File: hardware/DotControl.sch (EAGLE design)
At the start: 44 parts, among them CN1 1X4-BIG, IC1 MCP1703CB, J3 USB-MICROB, SW2 Previous, SW5 Previous, SW6 Next, SW8 Ok, U1 ATMEGA328P-MU-QFN32, U2 TMP102, U3 ATSHA204-TSU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

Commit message: Clean warnings
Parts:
- added C2: 1uF, rcl:C-EUC0603
- BAT1: value (none) -> 3V ML2032
- C1: value (none) -> 1uF
- D1, D2: value (none) -> MM5Z3V3
- R3, R4: value (none) -> 47Ω
- R5: value (none) -> 1.5kΩ
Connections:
- net +5V: now also C2.1
- net GND: now also C2.2
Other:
- moved on the sheet: SJ2
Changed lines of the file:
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@@
 <part name="+3V19" library="supply1" deviceset="+3V3" device=""/>
 <part name="P+4" library="supply1" deviceset="+5V" device=""/>
-<part name="C1" library="rcl" deviceset="C-EU" device="C0603"/>
+<part name="C1" library="rcl" deviceset="C-EU" device="C0603" value="1uF"/>
 <part name="JP3" library="adafruit" deviceset="PINHD-1X6" device=""/>
 <part name="+3V6" library="supply1" deviceset="+3V3" device=""/>
@@
 <part name="JP1" library="adafruit" deviceset="PINHD-1X8" device="CLEANBIG"/>
 <part name="SUPPLY8" library="supply2" deviceset="GND" device=""/>
-<part name="BAT1" library="Battery" deviceset="BATTERY" device="20PTH"/>
+<part name="BAT1" library="Battery" deviceset="BATTERY" device="20PTH" value="3V ML2032"/>
 <part name="+3V14" library="supply1" deviceset="+3V3" device=""/>
 <part name="LED1" library="led" deviceset="GM1WA55311A" device=""/>
@@
 <part name="SJ2" library="SparkFun" deviceset="SOLDERJUMPER" device="TRACE"/>
 <part name="+3V9" library="supply1" deviceset="+3V3" device=""/>
-<part name="D1" library="diode" deviceset="DIODE-" device="SOD523"/>
-<part name="D2" library="diode" deviceset="DIODE-" device="SOD523"/>
+<part name="D1" library="diode" deviceset="DIODE-" device="SOD523" value="MM5Z3V3"/>
+<part name="D2" library="diode" deviceset="DIODE-" device="SOD523" value="MM5Z3V3"/>
 <part name="SUPPLY14" library="supply2" deviceset="GND" device=""/>
-<part name="R3" library="rcl" deviceset="R-EU_" device="R0603"/>
-<part name="R4" library="rcl" deviceset="R-EU_" device="R0603"/>
-<part name="R5" library="rcl" deviceset="R-EU_" device="R0603"/>
+<part name="R3" library="rcl" deviceset="R-EU_" device="R0603" value="47Ω"/>
+<part name="R4" library="rcl" deviceset="R-EU_" device="R0603" value="47Ω"/>
+<part name="R5" library="rcl" deviceset="R-EU_" device="R0603" value="1.5kΩ"/>
 <part name="P+1" library="supply1" deviceset="+5V" device=""/>
 <part name="X1" library="adafruit" deviceset="ANTENNA_U.FL" device=""/>
@@
 <part name="Q1" library="adafruit" deviceset="MOSFET-N" device="REFLOW"/>
 <part name="IC1" library="linear" deviceset="MCP1703" device="CB"/>
+<part name="C2" library="rcl" deviceset="C-EU" device="C0603" value="1uF"/>
 </parts>
 <sheets>
@@
 <instance part="+3V10" gate="G$1" x="228.6" y="63.5"/>
 <instance part="SUPPLY5" gate="GND" x="228.6" y="53.34"/>
-<instance part="SJ2" gate="1" x="217.17" y="34.29" rot="R180"/>
+<instance part="SJ2" gate="1" x="422.91" y="240.03" rot="R180"/>
 <instance part="+3V9" gate="G$1" x="172.72" y="149.86"/>
 <instance part="D1" gate="G$1" x="322.58" y="99.06" rot="R90"/>
@@
 <instance part="Q1" gate="G$1" x="144.78" y="149.86" rot="R270"/>
 <instance part="IC1" gate="G$1" x="172.72" y="205.74"/>
+<instance part="C2" gate="G$1" x="160.02" y="203.2"/>
 </instances>
 <busses>
@@
 <wire x1="172.72" y1="198.12" x2="172.72" y2="195.58" width="0.1524" layer="91"/>
 <junction x="172.72" y="195.58"/>
+<pinref part="C2" gate="G$1" pin="2"/>
+<wire x1="160.02" y1="198.12" x2="160.02" y2="195.58" width="0.1524" layer="91"/>
+<wire x1="160.02" y1="195.58" x2="172.72" y2="195.58" width="0.1524" layer="91"/>
 </segment>
 <segment>
@@
 <pinref part="P+4" gate="1" pin="+5V"/>
 <wire x1="152.4" y1="210.82" x2="152.4" y2="205.74" width="0.1524" layer="91"/>
-<wire x1="152.4" y1="205.74" x2="162.56" y2="205.74" width="0.1524" layer="91"/>
+<wire x1="152.4" y1="205.74" x2="160.02" y2="205.74" width="0.1524" layer="91"/>
 <pinref part="IC1" gate="G$1" pin="VI"/>
+<pinref part="C2" gate="G$1" pin="1"/>
+<wire x1="160.02" y1="205.74" x2="162.56" y2="205.74" width="0.1524" layer="91"/>
+<junction x="160.02" y="205.74"/>
 </segment>
 <segment>
@@
 </sheet>
 </sheets>
+<errors>
+</errors>
 </schematic>
 </drawing>

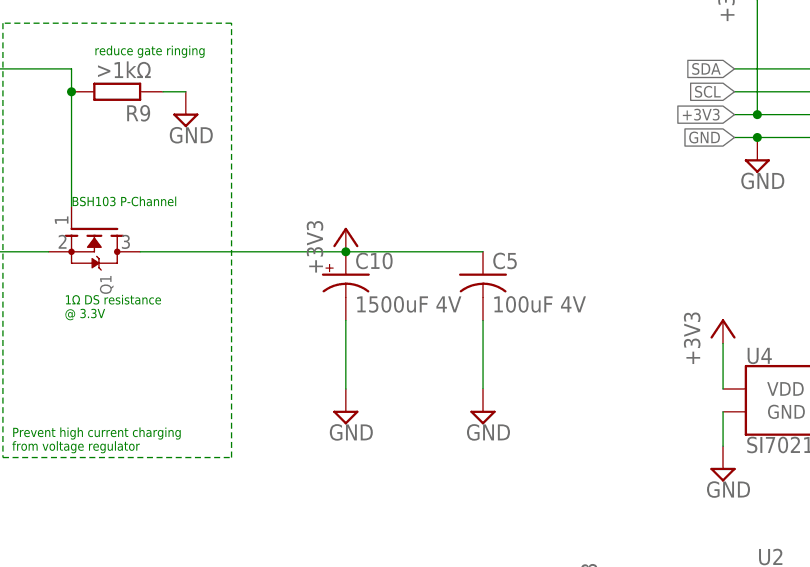
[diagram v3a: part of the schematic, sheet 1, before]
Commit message: 2x100uF instead of 1x1000uF
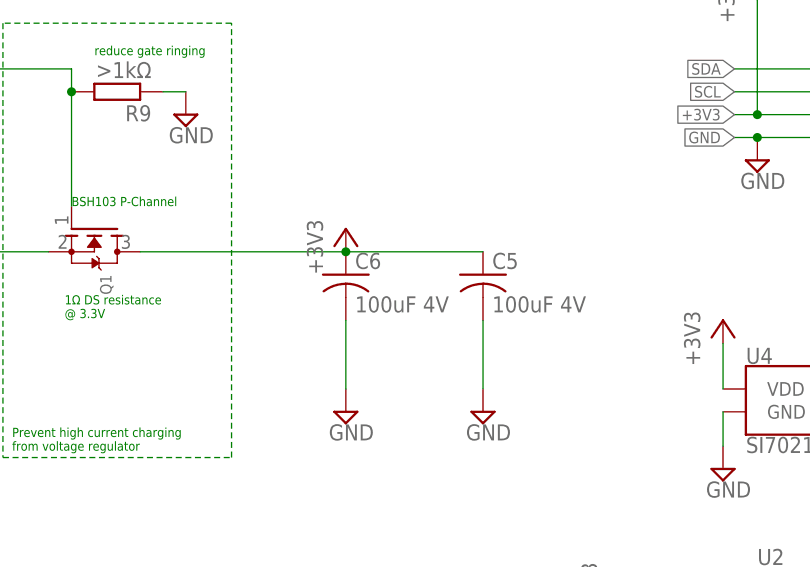
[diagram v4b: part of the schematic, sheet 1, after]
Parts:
- removed C10: 1500uF 4V, adafruit:CPOL-USCT7343
- added C6: 100uF 4V, adafruit:C-USC3216
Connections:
- net +3V3: now also C6.1; no longer C10.+
- net GND: now also C6.2; no longer C10.-
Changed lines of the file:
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@@
 <part name="+3V12" library="supply1" deviceset="+3V3" device=""/>
 <part name="SUPPLY11" library="supply2" deviceset="GND" device=""/>
-<part name="C10" library="adafruit" deviceset="CPOL-US" device="CT7343" value="1500uF 4V"/>
 <part name="SUPPLY16" library="supply2" deviceset="GND" device=""/>
 <part name="U5" library="SparkFun-Sensors" deviceset="MPU-9250" device="" value="9DoF IMU"/>
@@
 <part name="IC1" library="linear" deviceset="MCP1703" device="CB"/>
 <part name="C2" library="rcl" deviceset="C-EU" device="C0603" value="1uF"/>
+<part name="C6" library="adafruit" deviceset="C-US" device="C3216" value="100uF 4V"/>
 </parts>
 <sheets>
@@
 <instance part="+3V12" gate="G$1" x="214.63" y="139.7"/>
 <instance part="SUPPLY11" gate="GND" x="214.63" y="123.19"/>
-<instance part="C10" gate="G$1" x="172.72" y="144.78"/>
 <instance part="SUPPLY16" gate="GND" x="172.72" y="129.54"/>
 <instance part="U5" gate="G$1" x="525.78" y="220.98"/>
@@
 <instance part="IC1" gate="G$1" x="172.72" y="205.74"/>
 <instance part="C2" gate="G$1" x="160.02" y="203.2"/>
+<instance part="C6" gate="G$1" x="172.72" y="144.78"/>
 </instances>
 <busses>
@@
 </segment>
 <segment>
-<pinref part="C10" gate="G$1" pin="-"/>
 <pinref part="SUPPLY16" gate="GND" pin="GND"/>
 <wire x1="172.72" y1="139.7" x2="172.72" y2="132.08" width="0.1524" layer="91"/>
+<pinref part="C6" gate="G$1" pin="2"/>
 </segment>
 <segment>
@@
 <segment>
 <pinref part="+3V9" gate="G$1" pin="+3V3"/>
-<pinref part="C10" gate="G$1" pin="+"/>
 <junction x="172.72" y="147.32"/>
 <pinref part="C5" gate="G$1" pin="1"/>
@@
 <wire x1="149.86" y1="147.32" x2="172.72" y2="147.32" width="0.1524" layer="91"/>
 <pinref part="Q1" gate="G$1" pin="D"/>
-</segment>
-<segment>
+<pinref part="C6" gate="G$1" pin="1"/>
+</segment>
+<segment>

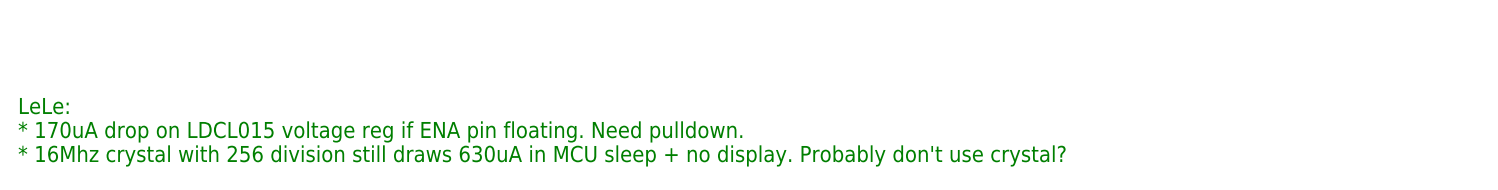
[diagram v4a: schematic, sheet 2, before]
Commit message: Update LeLe: 16Mhz with 256 divider = 5uA draw
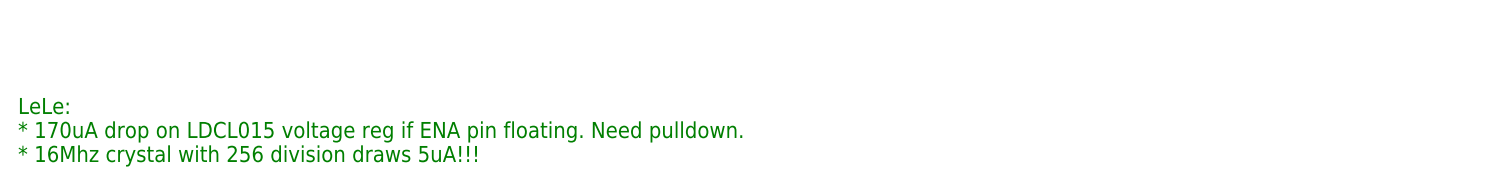
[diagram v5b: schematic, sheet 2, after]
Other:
- note added: "LeLe: * 170uA drop on LDCL015 voltage reg if ENA pin floating. Need pulldown. * 16Mhz crystal with 256 division draws 5uA!!!"
- note removed: "LeLe: * 170uA drop on LDCL015 voltage reg if ENA pin floating. Need pulldown. * 16Mhz crystal with 256 division still draws 630uA in MCU sleep + no display. Probably don't use crystal?"
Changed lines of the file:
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@@
 <text x="-17.78" y="86.36" size="1.778" layer="91">LeLe:
 * 170uA drop on LDCL015 voltage reg if ENA pin floating. Need pulldown.
-* 16Mhz crystal with 256 division still draws 630uA in MCU sleep + no display. Probably don't use crystal?</text>
+* 16Mhz crystal with 256 division draws 5uA!!!</text>
 </plain>
 <instances>

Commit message: Update LeLe: +/-0.3s / minute drift @ 16Mhz
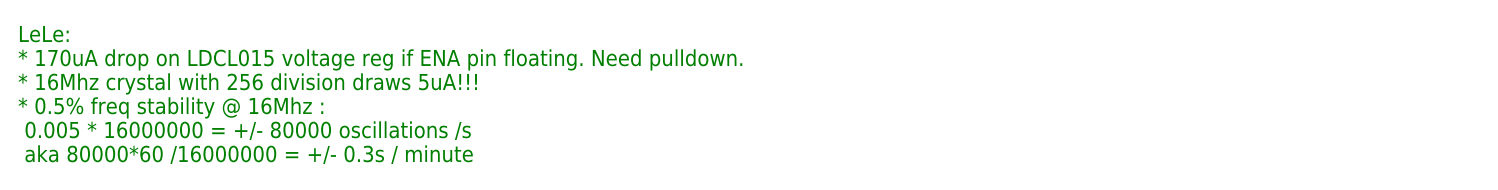
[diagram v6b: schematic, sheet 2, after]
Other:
- note added: "LeLe: * 170uA drop on LDCL015 voltage reg if ENA pin floating. Need pulldown. * 16Mhz crystal with 256 division draws 5uA!!! * 0.5% freq stability @ 16Mhz : 0.005 * 16000000 = +/- 80000 oscillations /s aka 80000*60 /16000000 = +/- 0.3s / minute"
- note removed: "LeLe: * 170uA drop on LDCL015 voltage reg if ENA pin floating. Need pulldown. * 16Mhz crystal with 256 division draws 5uA!!!"
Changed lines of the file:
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@@
 <text x="-17.78" y="86.36" size="1.778" layer="91">LeLe:
 * 170uA drop on LDCL015 voltage reg if ENA pin floating. Need pulldown.
-* 16Mhz crystal with 256 division draws 5uA!!!</text>
+* 16Mhz crystal with 256 division draws 5uA!!!
+* 0.5% freq stability @ 16Mhz :
+ 0.005 * 16000000 = +/- 80000 oscillations /s
+ aka 80000*60 /16000000 = +/- 0.3s / minute </text>
 </plain>
 <instances>

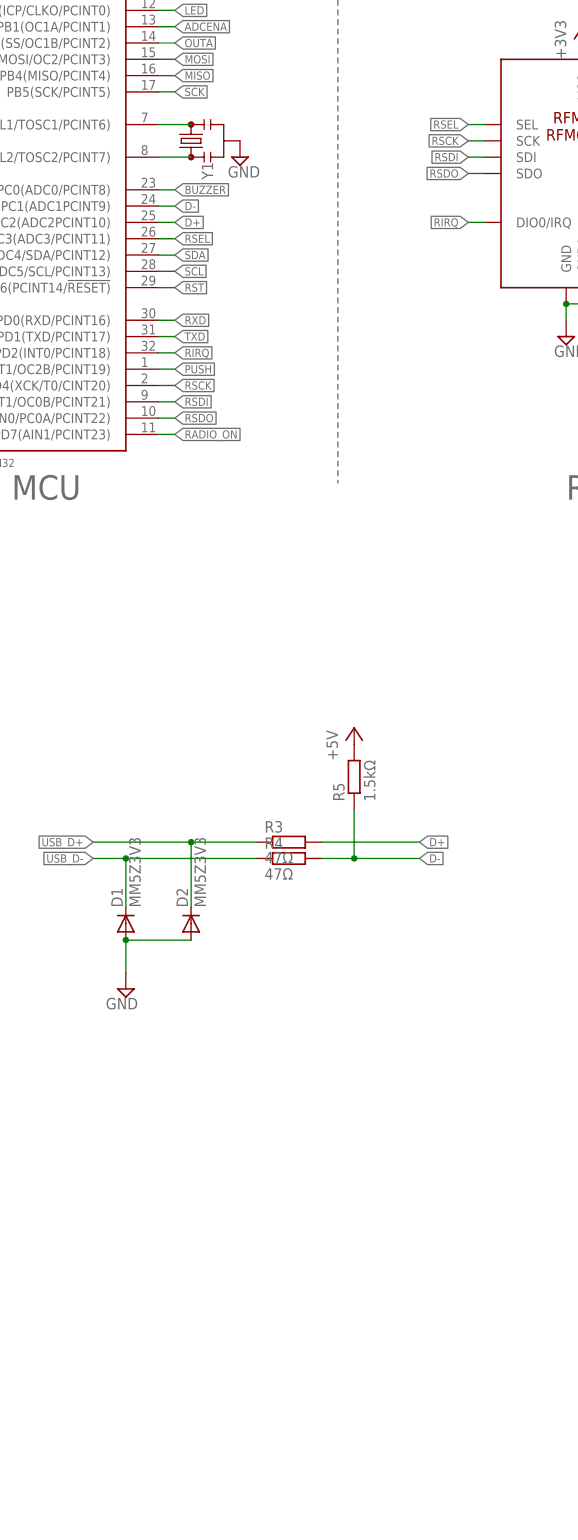
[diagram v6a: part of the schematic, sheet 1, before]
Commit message: Add support for 10ppm crystal
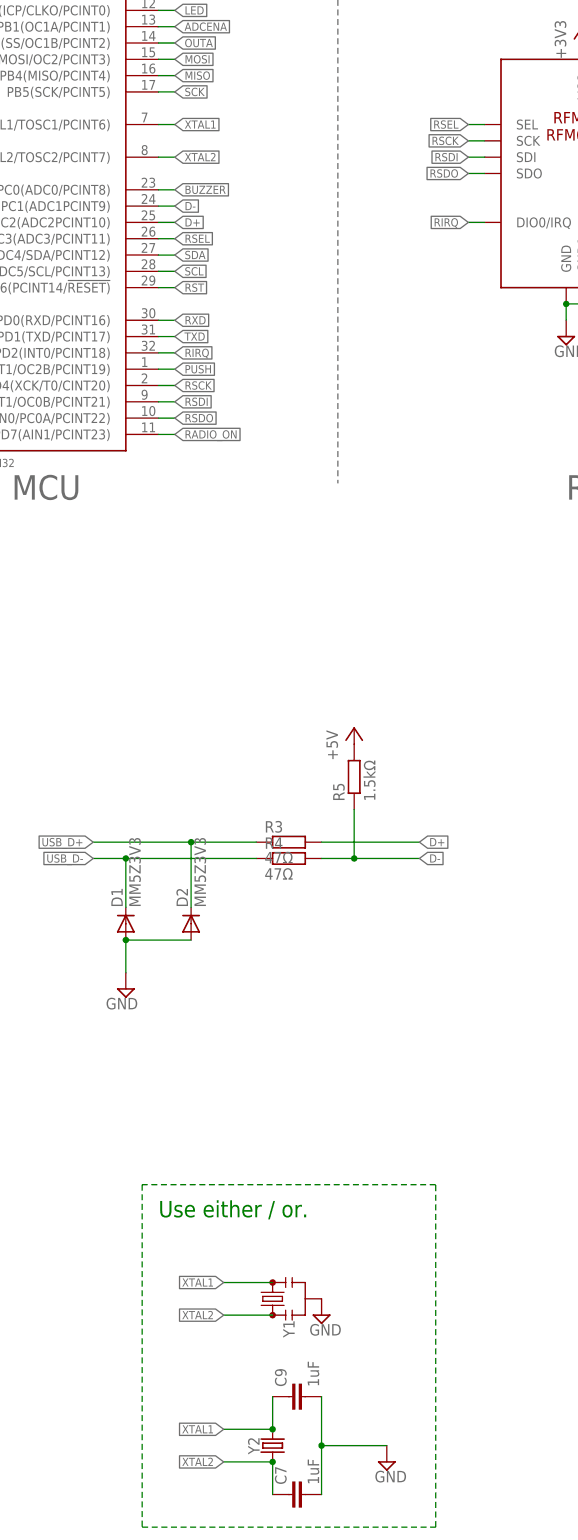
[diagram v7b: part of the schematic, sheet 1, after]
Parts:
- added C7, C9: 1uF, rcl:C-EUC0603
- added Y2: (no value), SparkFun-Clocks:CRYSTALSMD-3.2X1.5
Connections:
- removed net N$6: U1.PB6(XTAL1/TOSC1/PCINT6), Y1.3
- removed net N$8: U1.PB7(XTAL2/TOSC2/PCINT7), Y1.1
- new net XTAL1: C9.1, U1.PB6(XTAL1/TOSC1/PCINT6), Y1.3, Y2.2
- new net XTAL2: C7.1, U1.PB7(XTAL2/TOSC2/PCINT7), Y1.1, Y2.1
- net GND: now also C7.2, C9.2
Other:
- note added: "Use either / or."
- moved on the sheet: Y1
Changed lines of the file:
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@@
 <part name="C2" library="rcl" deviceset="C-EU" device="C0603" value="1uF"/>
 <part name="C6" library="adafruit" deviceset="C-US" device="C3216" value="100uF 4V"/>
+<part name="Y2" library="SparkFun-Clocks" deviceset="CRYSTAL" device="SMD-3.2X1.5"/>
+<part name="C7" library="rcl" deviceset="C-EU" device="C0603" value="1uF"/>
+<part name="C9" library="rcl" deviceset="C-EU" device="C0603" value="1uF"/>
+<part name="SUPPLY26" library="supply2" deviceset="GND" device=""/>
 </parts>
 <sheets>
@@
 <text x="141.478" y="139.954" size="1.016" layer="91">1Ω DS resistance
 @ 3.3V</text>
+<text x="327.66" y="53.34" size="2.54" layer="91">Use either / or.</text>
 </plain>
 <instances>
@@
 <instance part="+3V5" gate="G$1" x="393.7" y="238.76"/>
 <instance part="+3V2" gate="G$1" x="274.32" y="231.14" rot="R90"/>
-<instance part="Y1" gate="G$1" x="332.74" y="220.98" rot="R90"/>
-<instance part="SUPPLY30" gate="GND" x="340.36" y="218.44"/>
+<instance part="Y1" gate="G$1" x="345.44" y="40.64" rot="R90"/>
+<instance part="SUPPLY30" gate="GND" x="353.06" y="38.1"/>
 <instance part="SW2" gate="G$1" x="83.82" y="53.34" rot="R90"/>
 <instance part="JP1" gate="G$1" x="66.04" y="127" rot="MR270"/>
@@
 <instance part="C2" gate="G$1" x="160.02" y="203.2"/>
 <instance part="C6" gate="G$1" x="172.72" y="144.78"/>
+<instance part="Y2" gate="G$1" x="345.44" y="17.78" rot="R90"/>
+<instance part="C7" gate="G$1" x="347.98" y="10.16" rot="R90"/>
+<instance part="C9" gate="G$1" x="347.98" y="25.4" rot="R90"/>
+<instance part="SUPPLY26" gate="GND" x="363.22" y="15.24"/>
 </instances>
 <busses>
@@
 <pinref part="R9" gate="G$1" pin="1"/>
 <wire x1="154.94" y1="165.1" x2="152.4" y2="165.1" width="0.1524" layer="91"/>
+</segment>
+<segment>
+<pinref part="C9" gate="G$1" pin="2"/>
+<pinref part="C7" gate="G$1" pin="2"/>
+<wire x1="353.06" y1="25.4" x2="353.06" y2="17.78" width="0.1524" layer="91"/>
+<pinref part="SUPPLY26" gate="GND" pin="GND"/>
+<wire x1="353.06" y1="17.78" x2="353.06" y2="10.16" width="0.1524" layer="91"/>
+<wire x1="363.22" y1="17.78" x2="353.06" y2="17.78" width="0.1524" layer="91"/>
+<junction x="353.06" y="17.78"/>
 </segment>
 </net>
@@
 </segment>
 </net>
-<net name="N$6" class="0">
-<segment>
-<pinref part="U1" gate="G$1" pin="PB6(XTAL1/TOSC1/PCINT6)"/>
-<pinref part="Y1" gate="G$1" pin="3"/>
-<wire x1="332.74" y1="223.52" x2="327.66" y2="223.52" width="0.1524" layer="91"/>
-</segment>
-</net>
-<net name="N$8" class="0">
-<segment>
-<pinref part="U1" gate="G$1" pin="PB7(XTAL2/TOSC2/PCINT7)"/>
-<pinref part="Y1" gate="G$1" pin="1"/>
-<wire x1="332.74" y1="218.44" x2="327.66" y2="218.44" width="0.1524" layer="91"/>
-</segment>
-</net>
 <net name="RADIO_ON" class="0">
 <segment>
@@
 </segment>
 </net>
+<net name="XTAL1" class="0">
+<segment>
+<pinref part="Y1" gate="G$1" pin="3"/>
+<wire x1="345.44" y1="43.18" x2="337.82" y2="43.18" width="0.1524" layer="91"/>
+<label x="337.82" y="43.18" size="1.27" layer="95" rot="R180" xref="yes"/>
+</segment>
+<segment>
+<pinref part="C9" gate="G$1" pin="1"/>
+<pinref part="Y2" gate="G$1" pin="2"/>
+<wire x1="345.44" y1="25.4" x2="345.44" y2="20.32" width="0.1524" layer="91"/>
+<wire x1="345.44" y1="20.32" x2="337.82" y2="20.32" width="0.1524" layer="91"/>
+<junction x="345.44" y="20.32"/>
+<label x="337.82" y="20.32" size="1.27" layer="95" rot="R180" xref="yes"/>
+</segment>
+<segment>
+<pinref part="U1" gate="G$1" pin="PB6(XTAL1/TOSC1/PCINT6)"/>
+<wire x1="327.66" y1="223.52" x2="330.2" y2="223.52" width="0.1524" layer="91"/>
+<label x="330.2" y="223.52" size="1.27" layer="95" xref="yes"/>
+</segment>
+</net>
+<net name="XTAL2" class="0">
+<segment>
+<pinref part="Y1" gate="G$1" pin="1"/>
+<wire x1="345.44" y1="38.1" x2="337.82" y2="38.1" width="0.1524" layer="91"/>
+<label x="337.82" y="38.1" size="1.27" layer="95" rot="R180" xref="yes"/>
+</segment>
+<segment>
+<pinref part="Y2" gate="G$1" pin="1"/>
+<pinref part="C7" gate="G$1" pin="1"/>
+<wire x1="345.44" y1="15.24" x2="345.44" y2="10.16" width="0.1524" layer="91"/>
+<wire x1="345.44" y1="15.24" x2="337.82" y2="15.24" width="0.1524" layer="91"/>
+<junction x="345.44" y="15.24"/>
+<label x="337.82" y="15.24" size="1.27" layer="95" rot="R180" xref="yes"/>
+</segment>
+<segment>
+<pinref part="U1" gate="G$1" pin="PB7(XTAL2/TOSC2/PCINT7)"/>
+<wire x1="327.66" y1="218.44" x2="330.2" y2="218.44" width="0.1524" layer="91"/>
+<label x="330.2" y="218.44" size="1.27" layer="95" xref="yes"/>
+</segment>
+</net>
+<net name="N$6" class="0">
+<segment>
+<wire x1="325.12" y1="58.42" x2="325.12" y2="5.08" width="0.1524" layer="91" style="longdash"/>
+<wire x1="325.12" y1="5.08" x2="370.84" y2="5.08" width="0.1524" layer="91" style="longdash"/>
+<wire x1="370.84" y1="5.08" x2="370.84" y2="58.42" width="0.1524" layer="91" style="longdash"/>
+<wire x1="370.84" y1="58.42" x2="325.12" y2="58.42" width="0.1524" layer="91" style="longdash"/>
+</segment>
+</net>
